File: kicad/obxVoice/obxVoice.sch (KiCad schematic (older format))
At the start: 197 parts, among them T1 100k, T11 100k, T2 10k, T3 10k, T4 100k, T5 10k, T6 10k, T7 10k, T8 10k

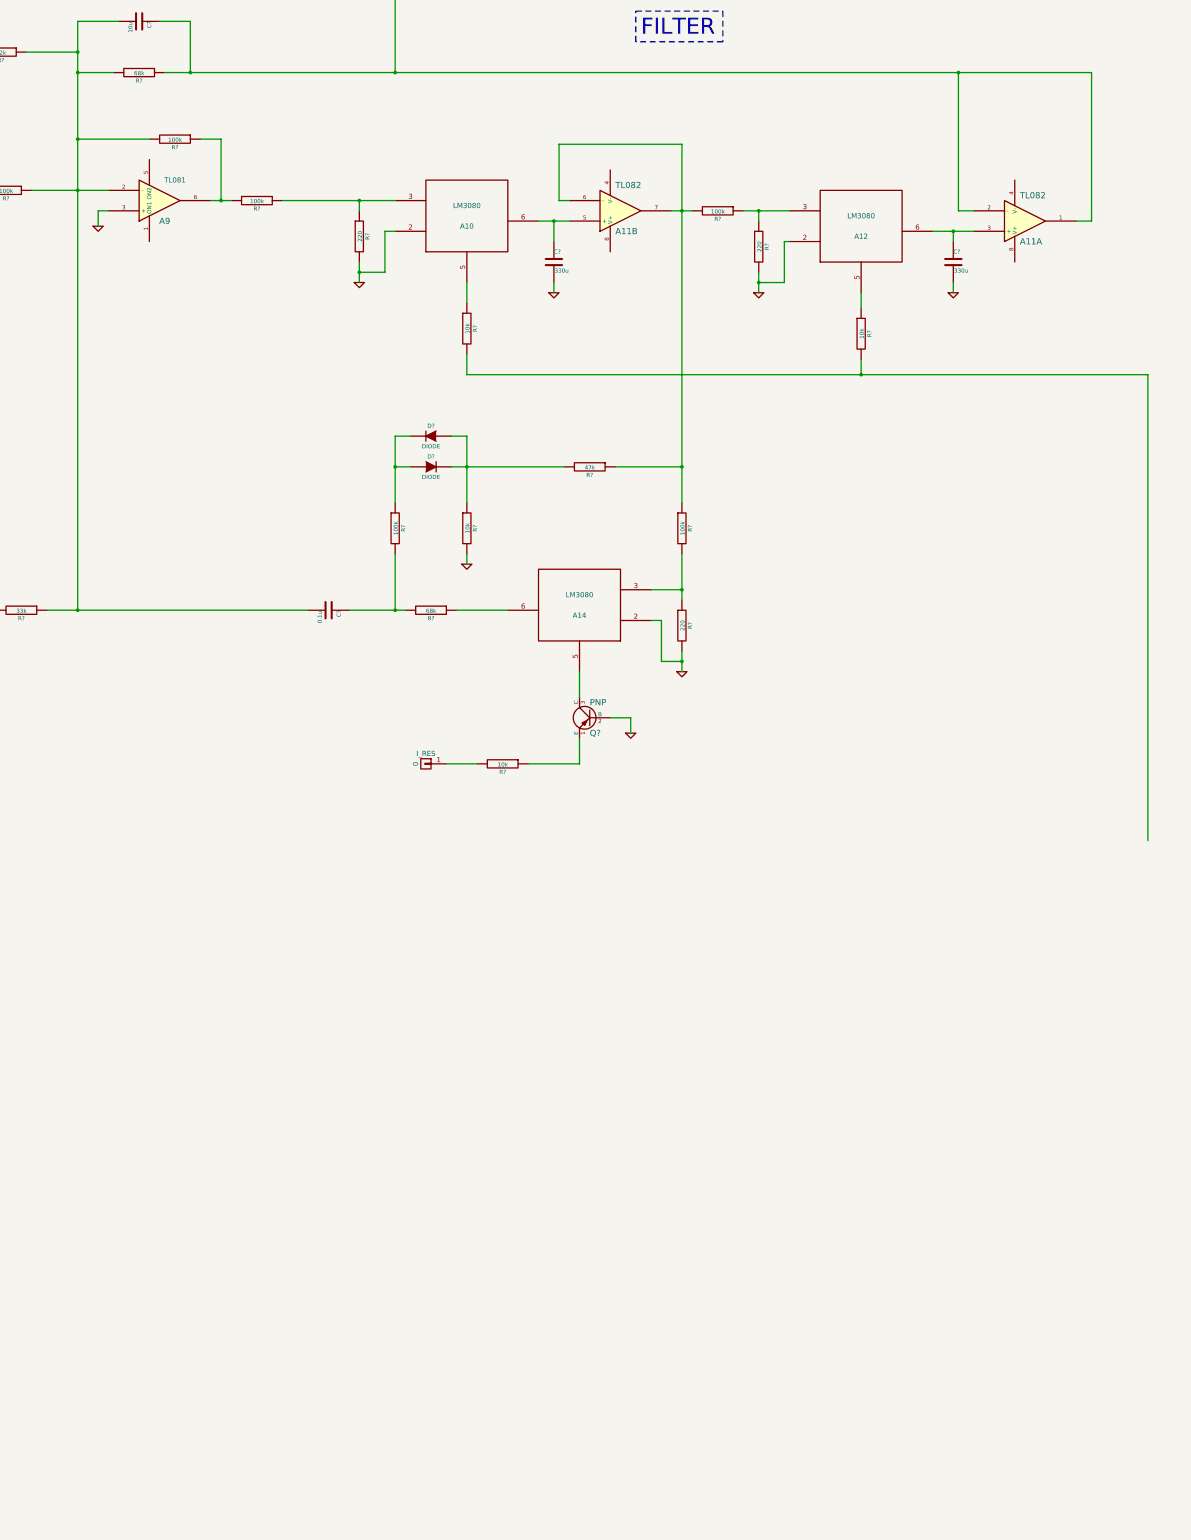
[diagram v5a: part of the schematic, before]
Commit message: The Filter Envelope region is nearly complete for the OBX.
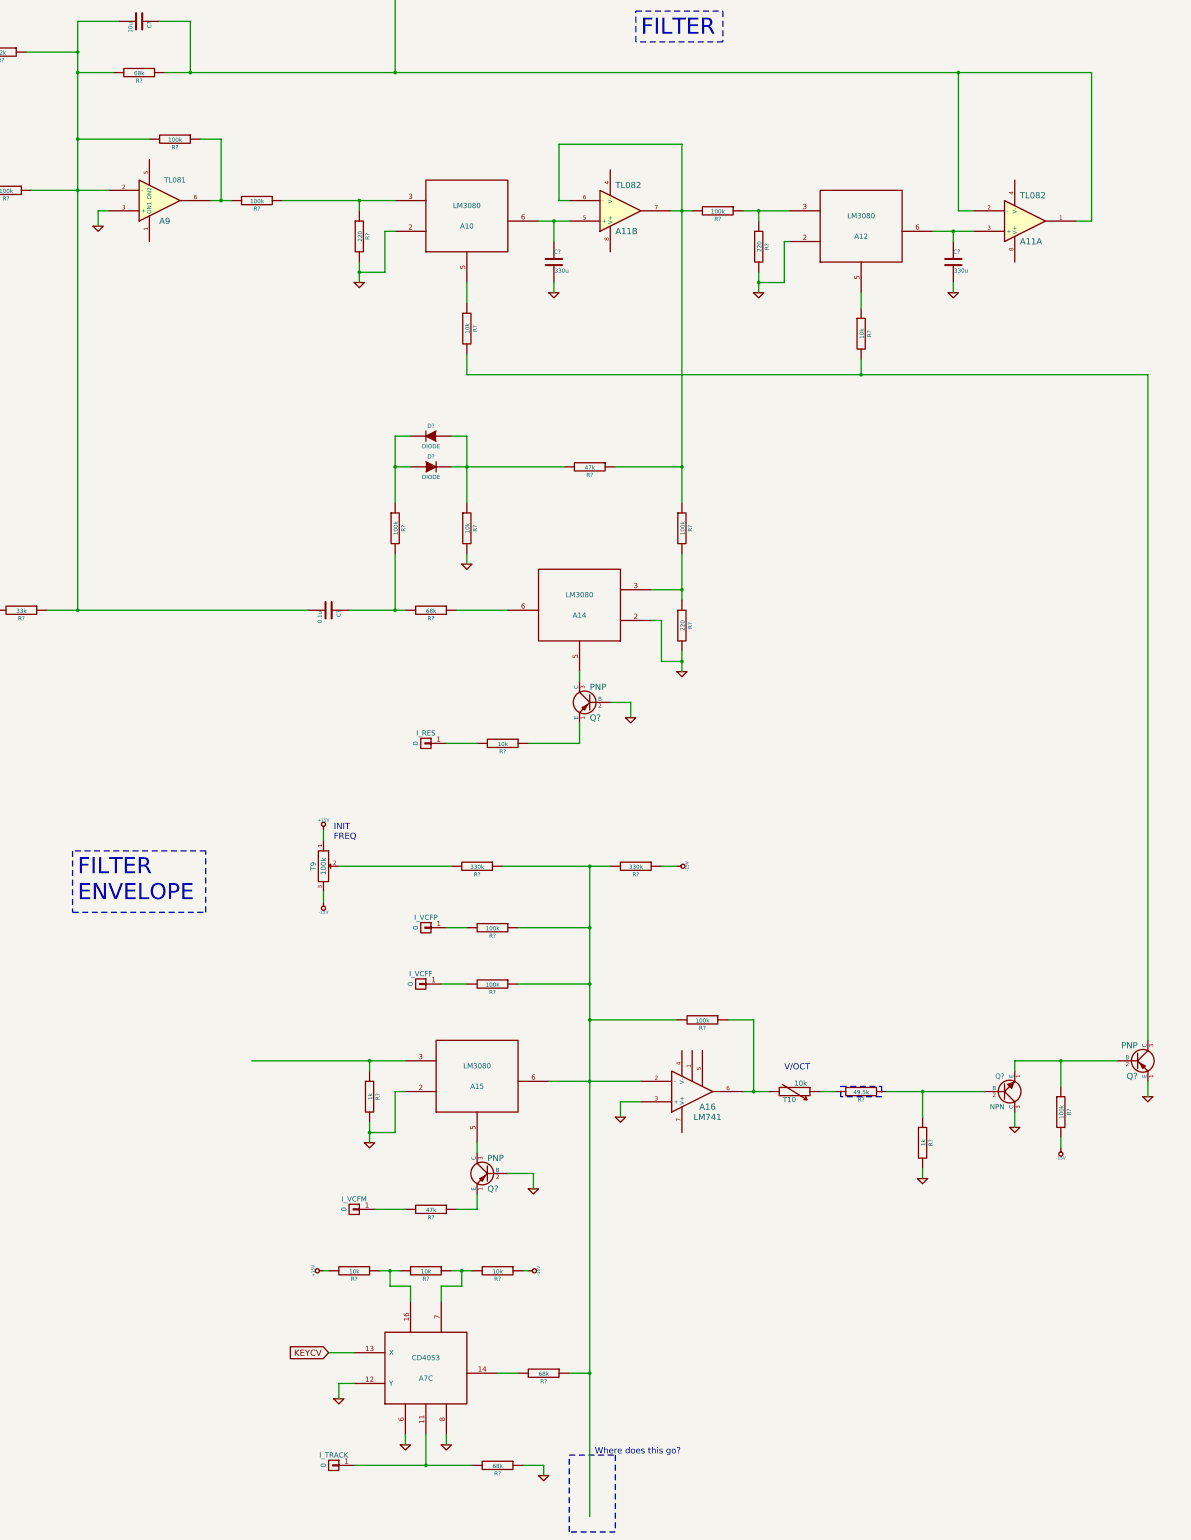
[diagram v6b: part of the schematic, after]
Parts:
- added A15: LM3080, symbol LM3080
- added A16: LM741, symbol LM741
- added unit 3 of A7
- added I_TRACK, I_VCFF, I_VCFM, I_VCFP: 0, symbol CONN_01X01
- added Q? (x2): PNP, symbol PNP
- added Q?: NPN, symbol NPN
- added R? (x4): 100k, symbol R
- added R? (x2): 1k, symbol R
- added R?: 49.5k, symbol R
- added R?: 47k, symbol R
- added R? (x2): 68k, symbol R
- added R? (x3): 10k, symbol R
- added R? (x2): 330k, symbol R
- added T10: 10k, symbol RVAR
- added T9: 100k, symbol POT
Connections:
- net +15V: now also R?.2, T9.1
- net -15V: now also R?.1, R?.1, R?.2, T9.3
- net GND: now also A15.2, A16.3 (+), A7.12 (Y), A7.6, A7.8, Q?.1 (E), Q?.2 (B), Q?.3 (C), R?.1, R?.2, R?.2
- net KEYCV: now also A7.13 (X)
- net at R?.2, R?.2: now also Q?.3 (C)
- new net: Q?.1 (E), Q?.2 (B), R?.1
- new net: Q?.2 (B), R?.1, R?.1
- new net: R?.2, T10.1
- new net: A16.6, R?.1, T10.2
- new net: A15.6, A16.2 (-), R?.1, R?.1, R?.1, R?.1, R?.2, R?.2
- new net: A15.3, R?.1
- new net: A15.5, Q?.3 (C)
- new net: Q?.1 (E), R?.1
- new net: I_VCFM.1 (P1), R?.2
- new net: A7.11, I_TRACK.1 (P1), R?.2
- new net: A7.14, R?.2
- new net: A7.16, R?.1, R?.2
- new net: A7.7, R?.1, R?.2
- new net: I_VCFF.1 (P1), R?.2
- new net: I_VCFP.1 (P1), R?.2
- new net: R?.2, T9.2
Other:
- note added: "FILTER\nENVELOPE"
- note added: "V/OCT"
- note added: "Where does this go?"
- moved on the sheet: I_RES, Q?, R?

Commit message: The OBX is complete, barring any nasty bugs.
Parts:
- added A18, A19: CEM3310, symbol CEM3310
- added C? (x2): 0.022u, symbol C
- added C? (x2): 0.047u, symbol C
- added C? (x2): 0.001u, symbol C
- added I_AATK, I_AATK?, I_ADCY, I_ADCY?, I_ARLS, I_ARLS?, I_ASUS, I_ASUS?, I_GATE: 0, symbol CONN_01X01
- added R? (x2): 24k, symbol R
- added R? (x2): 680, symbol R
- added R? (x8): 10, symbol R
- added R?: 47k, symbol R
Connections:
- net +15V: now also A18.11, A19.11
- net -15V: now also R?.2, R?.2
- net GND: now also A18.14, A18.7, A19.14, A19.7, C?.1, C?.1, C?.1, C?.1
- net at R?.2: now also A19.2, R?.1
- net at A15.3, R?.1: now also R?.1
- new net: A19.1, C?.2
- new net: A19.10, R?.2
- new net: A19.12, R?.1
- new net: A19.13, R?.1
- new net: A19.15, R?.1
- new net: A19.5, C?.2
- new net: A19.6, R?.1
- new net: A19.8, C?.2
- new net: A19.9, R?.1
- new net: I_AATK.1 (P1), R?.2
- new net: I_ADCY.1 (P1), R?.2
- new net: I_ARLS.1 (P1), R?.2
- new net: I_ASUS.1 (P1), R?.2
- new net: A18.1, C?.2
- new net: A18.10, R?.2
- new net: A18.12, R?.1
- new net: A18.13, R?.1
- new net: A18.15, R?.1
- new net: A18.2, R?.1, R?.2
- new net: A18.4, C?.1, I_GATE.1 (P1)
- new net: A18.6, R?.1
- new net: A18.8, C?.2
- new net: A18.9, R?.1
- new net: I_AATK?.1 (P1), R?.2
- new net: I_ADCY?.1 (P1), R?.2
- new net: I_ARLS?.1 (P1), R?.2
- new net: I_ASUS?.1 (P1), R?.2
- new net GATE: A18.5, A19.4, C?.1, C?.2
